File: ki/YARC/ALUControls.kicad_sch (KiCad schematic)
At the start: 11 parts, among them U123 74LS32, U124 74LS08, U125 74LS08, U126 74LS08, U127 74LS74, U129 74LS574, U130 74LS157, U131 74LS245, U136 74LS32, U137 74HC00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

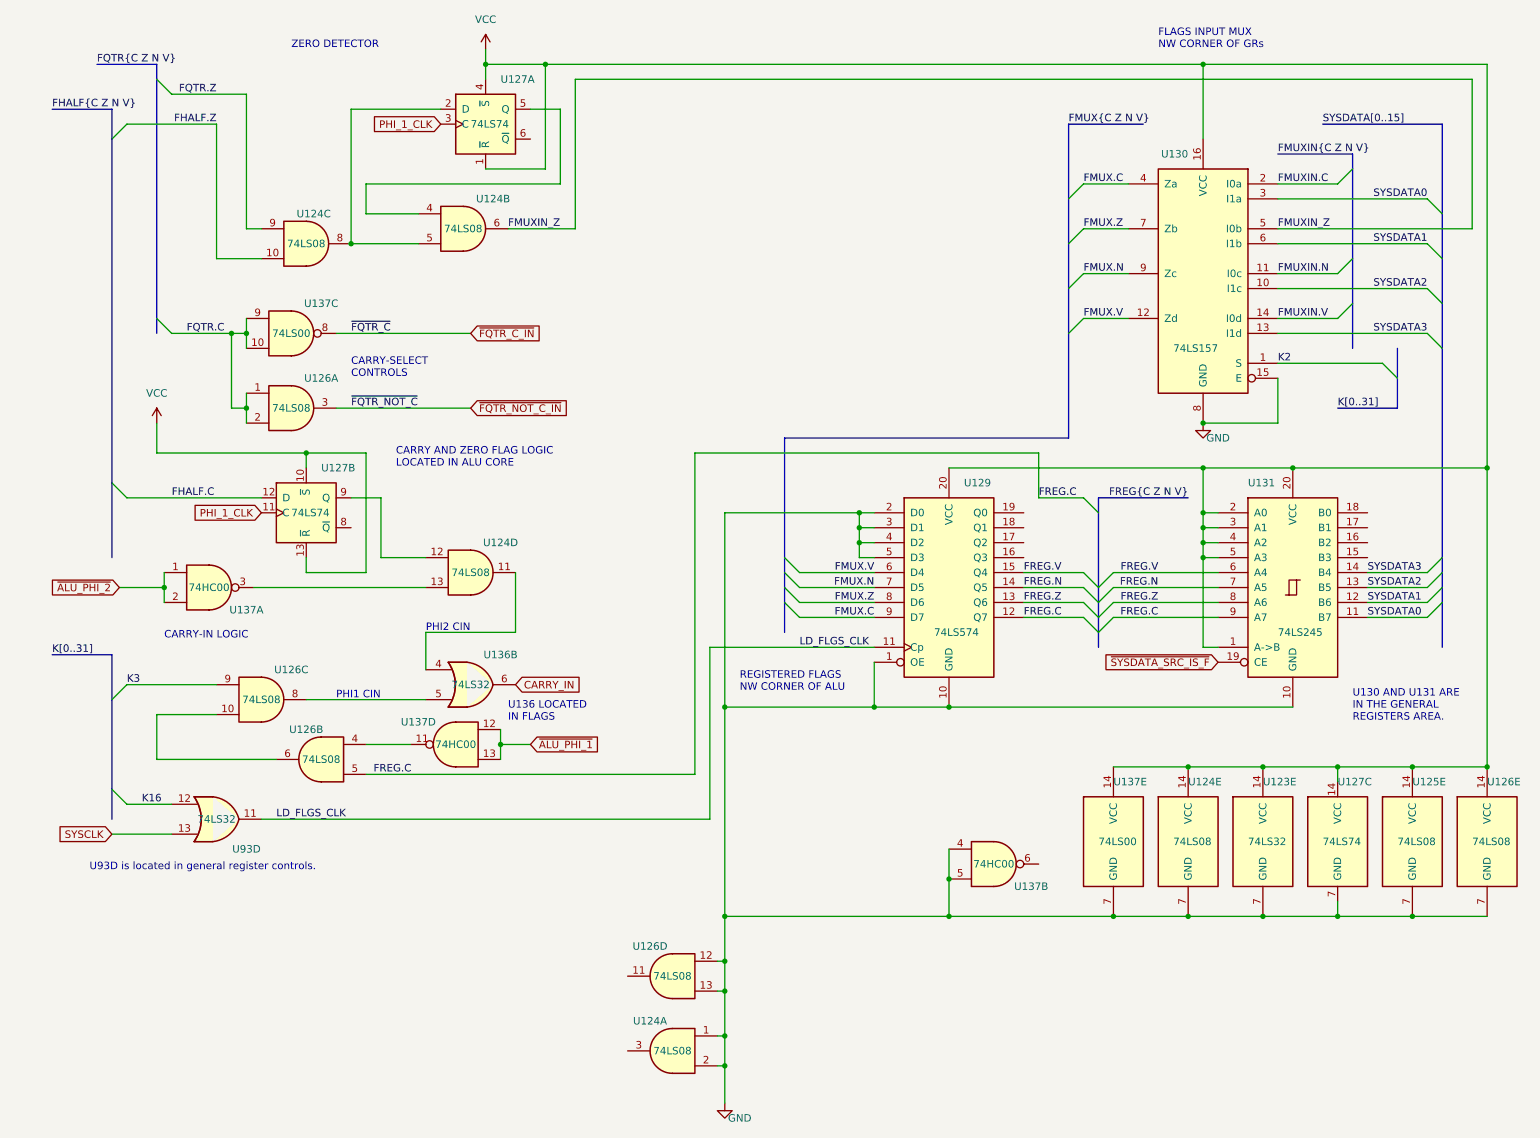
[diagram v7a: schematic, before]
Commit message: Convert schematic to KiCad 7
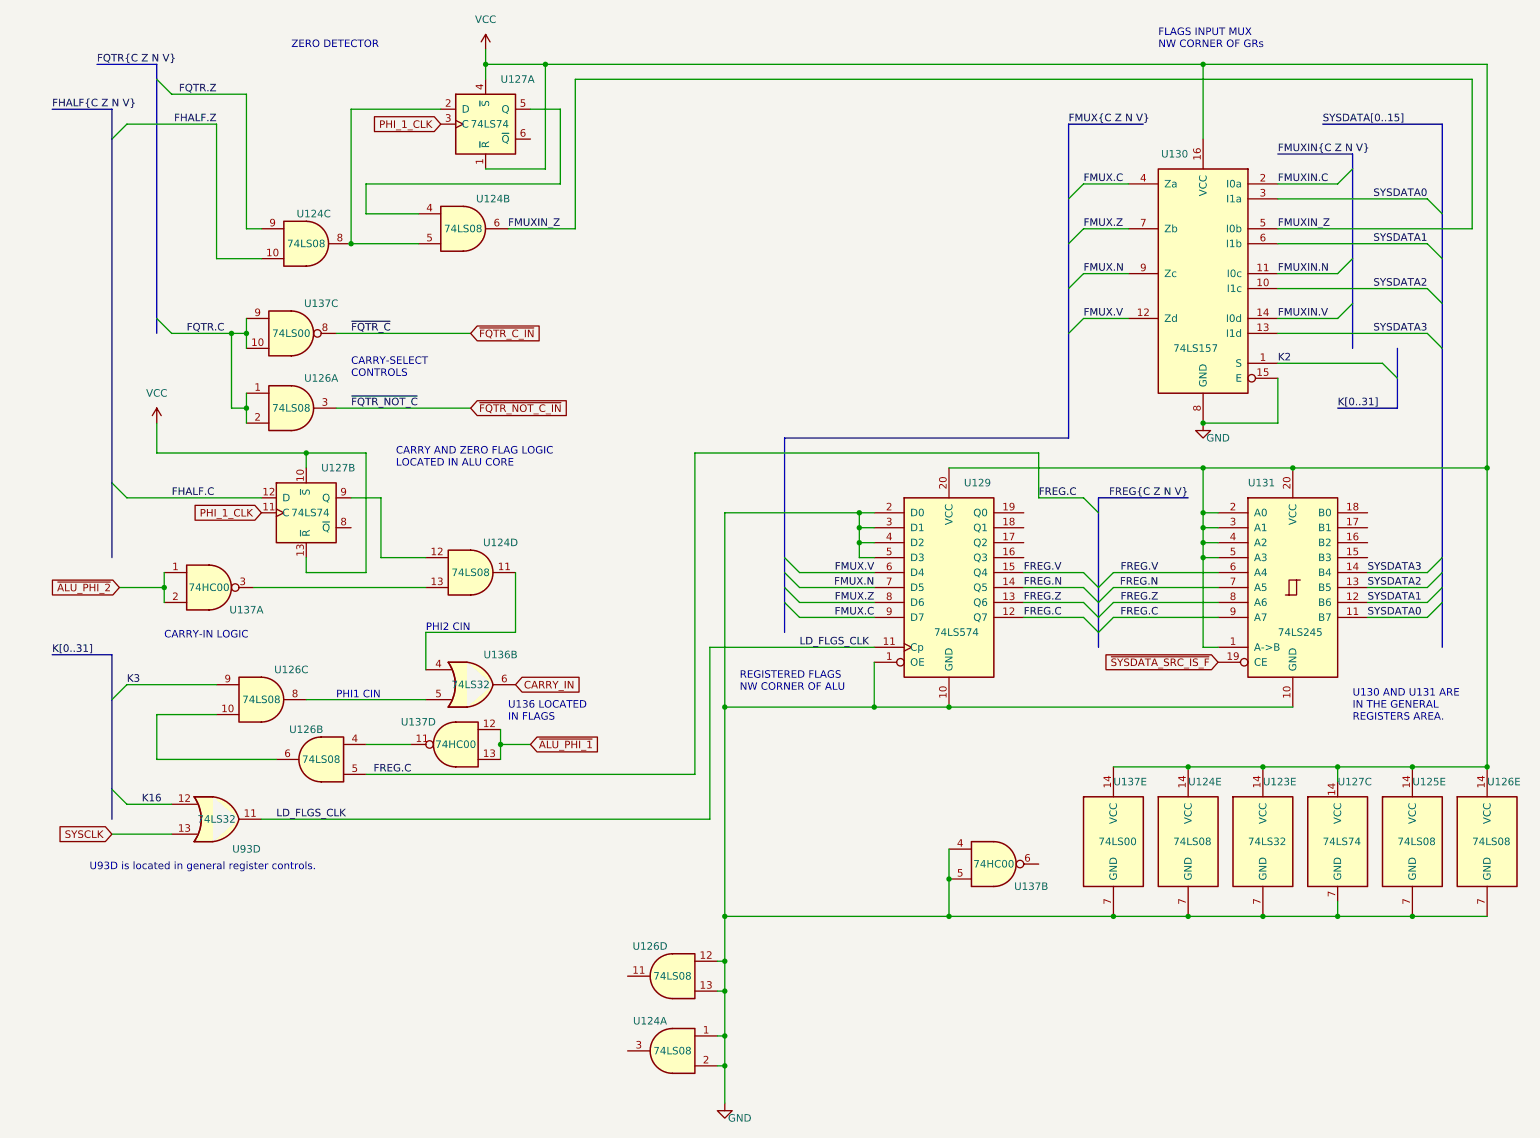
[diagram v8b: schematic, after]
